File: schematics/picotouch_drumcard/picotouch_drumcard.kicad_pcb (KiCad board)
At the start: 2 copper layers, 88.9 x 63.5 mm, 80 parts, among them J1 AudioJack4, J2 AudioJack4, J3 AudioJack4, SW1 Capacitive Button, SW10 Capacitive Button, SW11 Capacitive Button, SW12 Capacitive Button, SW13 Capacitive Button, SW14 Capacitive Button, SW15 Capacitive Button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

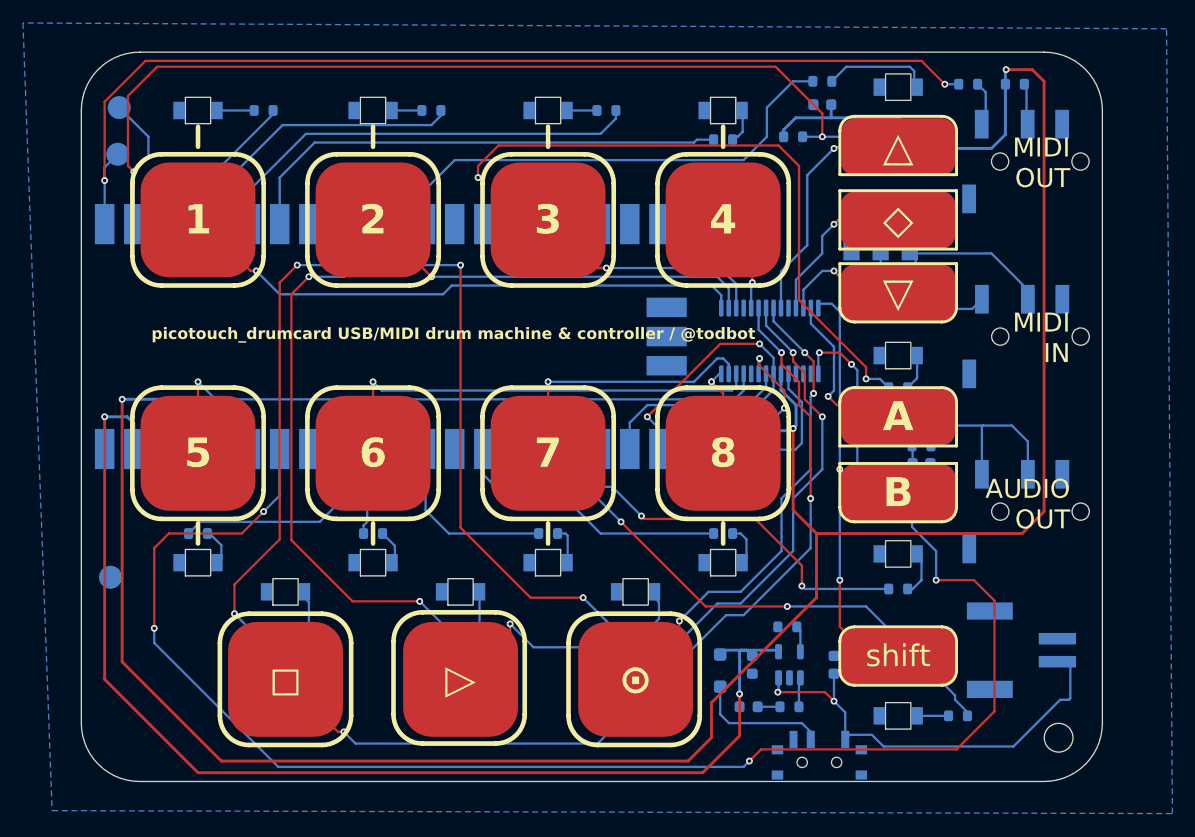
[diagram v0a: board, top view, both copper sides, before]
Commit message: audio out needs Ring2 to Gnd for headphones to work (I knew this)
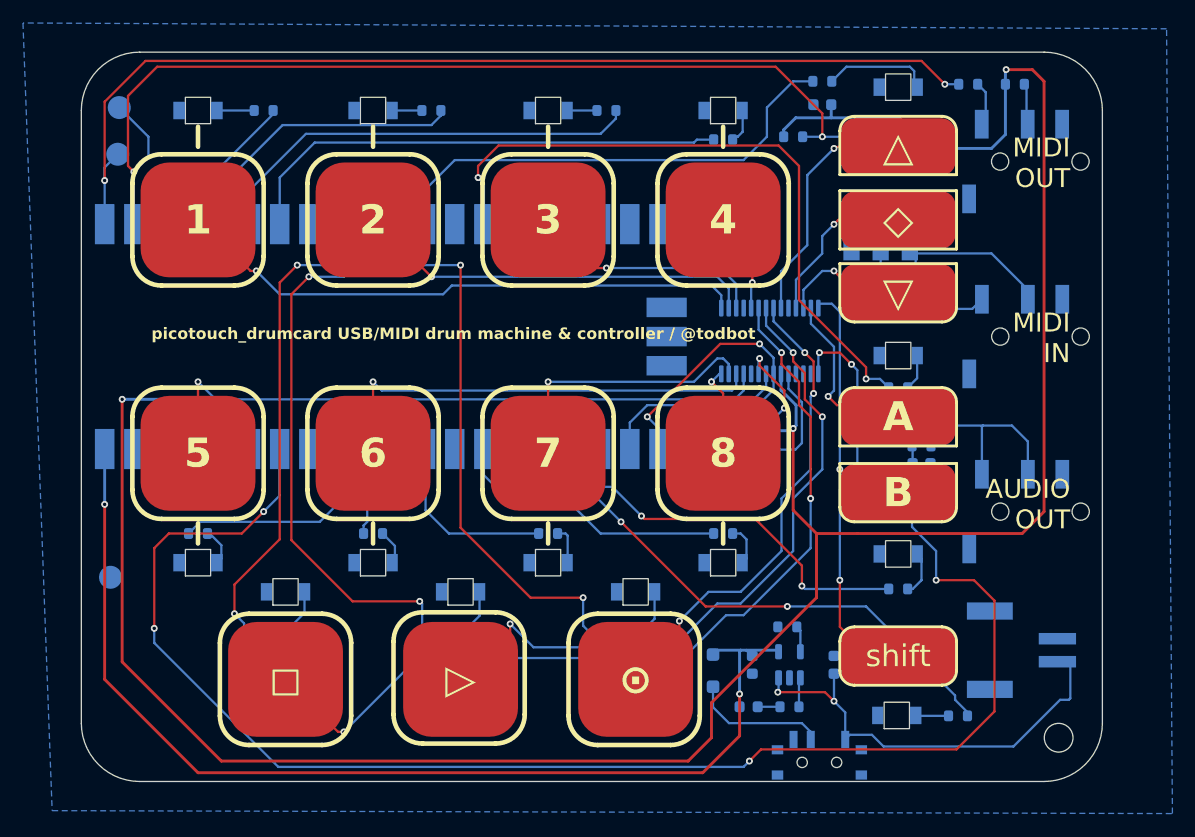
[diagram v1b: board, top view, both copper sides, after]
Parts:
- moved R9 2.79 mm to (116.6, 64.0)
- moved R10 2.62 mm to (132.1, 64.0)
- moved R11 2.26 mm to (147.6, 63.2)
- moved D18 0.63 mm to (156.6, 66.5)
- moved D15 0.13 mm to (172.6, 70.5)
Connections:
- J3 pad R2: unconnected-(J3-PadR2) -> GND
- U1 pad 39: +5V -> unconnected-(U1-VSYS-Pad39)
- U1 pad 40: unconnected-(U1-VBUS-Pad40) -> +5V
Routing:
- net +5V: track 102.1 -> 96.2 mm
- net Net-(D10-A): track 3.39 -> 5.83 mm
- net /LED9: track 42.8 -> 40.9 mm
- net Net-(D11-A): track 3.71 -> 5.43 mm
- net Net-(D9-A): track 4.41 -> 6.12 mm
- net /TOUCH9: track 78.2 -> 77.4 mm
- net /LED11: track 48.7 -> 47.9 mm
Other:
- board text added: "picotouch_drumcard Aug 2024 - @todbot / Tod Kurt github.com/todbot/picotouch_drumcard"
- board text removed: "picotouch_drumcard 2 Aug 2024 - @todbot / Tod Kurt github.com/todbot/picotouch_drumcard"
